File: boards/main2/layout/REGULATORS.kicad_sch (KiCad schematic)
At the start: 32 parts, among them IC7 L6981C33DR, J1 B02B-PASK(LF)(SN), Q6 HSBB3072, Q8 AO3401A, SW4 MK-12D18-G040, U8 ADP7142ACPZN3.3-R7, U9 INA228AIDGSR

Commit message: 🎨 Place main2's REGULATORS sheet
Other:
- note added: "3V3_A analog LDO: ADP7142, RC-filtered input"
- note added: "3V3_D buck: L6981C33, fixed 3.3 V"
- note added: "Battery current monitor: shunt R59, INA228 on the ESP32's I2C"
- note added: "Battery input and switch: SW4 drives the low-side MOSFET Q6"
- note added: "Battery voltage to the ADC"
- note added: "Power path: VSYS = VBAT or VBUS"
- note added: "Sheet ports"
- title: (none) -> Battery input, power path and regulators
- moved on the sheet: C52, C53, C54, C55, C56, C57, C58, C59, C63, C80, C81, C90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

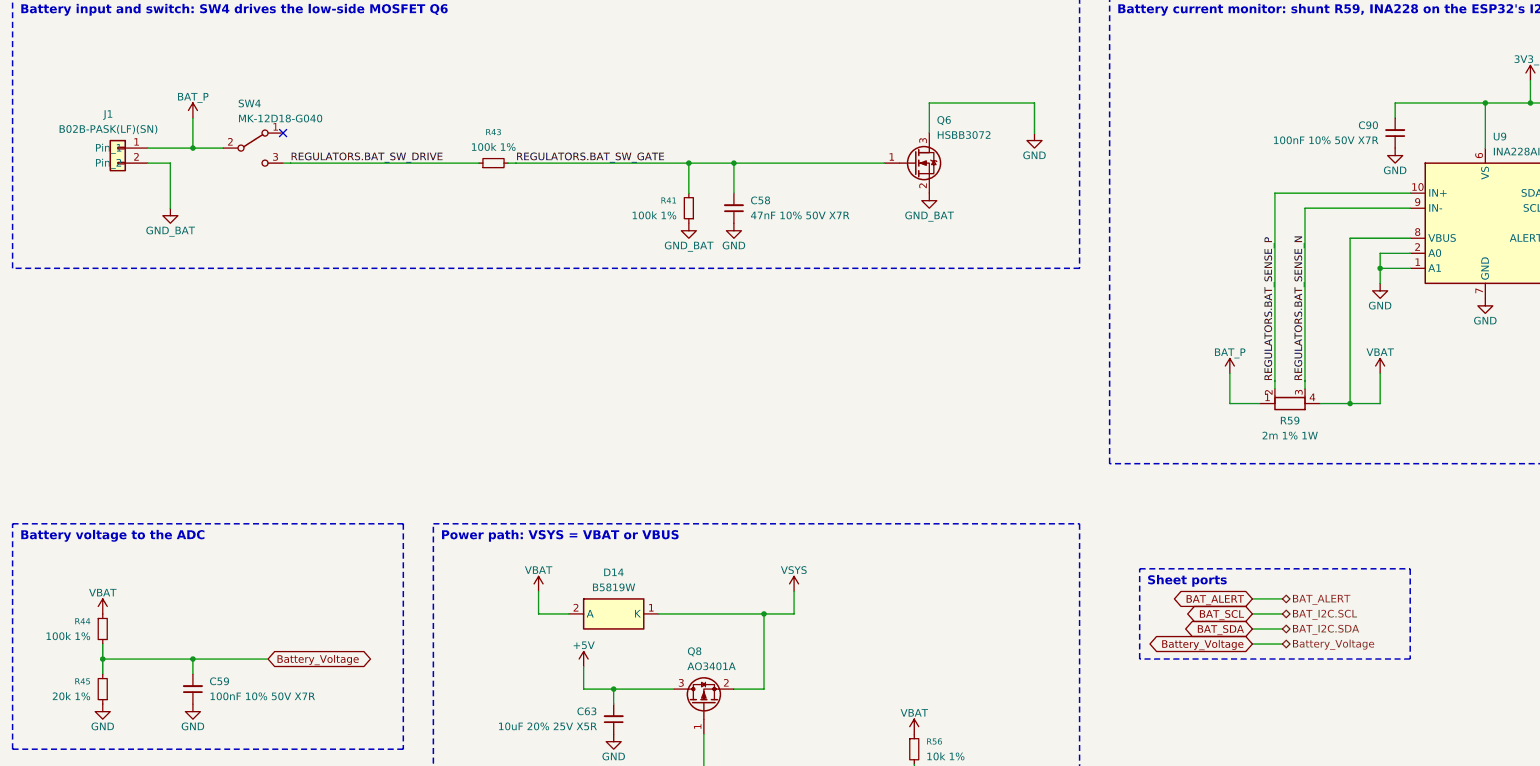
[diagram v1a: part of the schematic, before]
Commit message: 🎨 Place main2's SENSORS sheet, and draw the TLV9001's inputs as + and − in its triangle
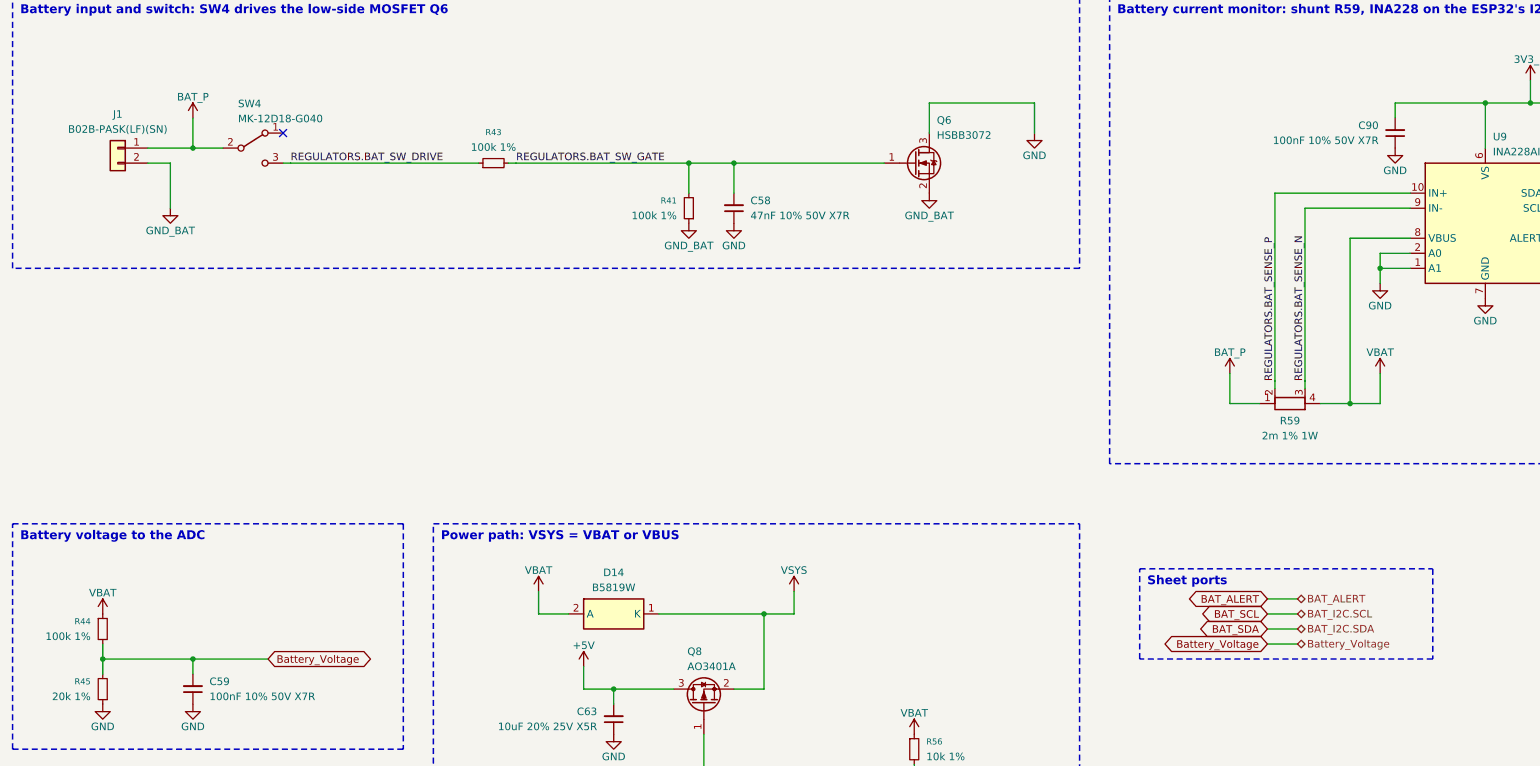
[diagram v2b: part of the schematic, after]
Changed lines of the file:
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@@
 		(dnp no)
 		(property "Reference" "J1"
-			(at 28.8955 34.925 0)
+			(at 30.48 34.925 0)
 			(show_name no)
 			(do_not_autoplace no)
@@
 		)
 		(property "Value" "B02B-PASK(LF)(SN)"
-			(at 28.8955 37.465 0)
+			(at 30.48 37.465 0)
 			(show_name no)
 			(do_not_autoplace no)
@@
 	(wire
 		(pts
-			(xy 222.25 116.84) (xy 227.33 116.84)
+			(xy 224.79 116.84) (xy 229.87 116.84)
 		)
 		(stroke
@@
 	(wire
 		(pts
-			(xy 222.25 119.38) (xy 227.33 119.38)
+			(xy 224.79 119.38) (xy 229.87 119.38)
 		)
 		(stroke
@@
 	(wire
 		(pts
-			(xy 222.25 121.92) (xy 227.33 121.92)
+			(xy 224.79 121.92) (xy 229.87 121.92)
 		)
 		(stroke
@@
 	(wire
 		(pts
-			(xy 222.25 124.46) (xy 227.33 124.46)
+			(xy 224.79 124.46) (xy 229.87 124.46)
 		)
 		(stroke
@@
 	(global_label "BAT_ALERT"
 		(shape bidirectional)
-		(at 222.25 116.84 180)
+		(at 224.79 116.84 180)
 		(effects
 			(font
@@
 		)
 		(property "Intersheetrefs" "${INTERSHEET_REFS}"
-			(at 222.25 116.84 0)
+			(at 224.79 116.84 0)
 			(hide yes)
 			(show_name no)
@@
 	(hierarchical_label "BAT_ALERT"
 		(shape bidirectional)
-		(at 227.33 116.84 0)
+		(at 229.87 116.84 0)
 		(effects
 			(font
@@
 	(global_label "BAT_SCL"
 		(shape bidirectional)
-		(at 222.25 119.38 180)
+		(at 224.79 119.38 180)
 		(effects
 			(font
@@
 		)
 		(property "Intersheetrefs" "${INTERSHEET_REFS}"
-			(at 222.25 119.38 0)
+			(at 224.79 119.38 0)
 			(hide yes)
 			(show_name no)
@@
 	(hierarchical_label "BAT_I2C.SCL"
 		(shape bidirectional)
-		(at 227.33 119.38 0)
+		(at 229.87 119.38 0)
 		(effects
 			(font
@@
 	(global_label "BAT_SDA"
 		(shape bidirectional)
-		(at 222.25 121.92 180)
+		(at 224.79 121.92 180)
 		(effects
 			(font
@@
 		)
 		(property "Intersheetrefs" "${INTERSHEET_REFS}"
-			(at 222.25 121.92 0)
+			(at 224.79 121.92 0)
 			(hide yes)
 			(show_name no)
@@
 	(hierarchical_label "BAT_I2C.SDA"
 		(shape bidirectional)
-		(at 227.33 121.92 0)
+		(at 229.87 121.92 0)
 		(effects
 			(font
@@
 	(global_label "Battery_Voltage"
 		(shape bidirectional)
-		(at 222.25 124.46 180)
+		(at 224.79 124.46 180)
 		(effects
 			(font
@@
 		)
 		(property "Intersheetrefs" "${INTERSHEET_REFS}"
-			(at 222.25 124.46 0)
+			(at 224.79 124.46 0)
 			(hide yes)
 			(show_name no)
@@
 	(hierarchical_label "Battery_Voltage"
 		(shape bidirectional)
-		(at 227.33 124.46 0)
+		(at 229.87 124.46 0)
 		(effects
 			(font
@@
 	(rectangle
 		(start 203.2 111.76)
-		(end 248.92 127)
+		(end 252.73 127)
 		(stroke
 			(width 0.254)

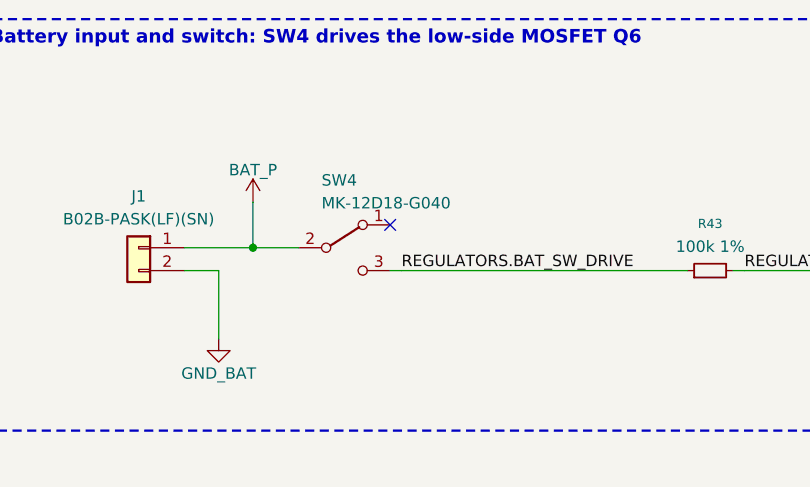
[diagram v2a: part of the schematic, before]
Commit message: 🔧 Switch main2's battery on the SK-12D29-G060, rated for the 4S pack
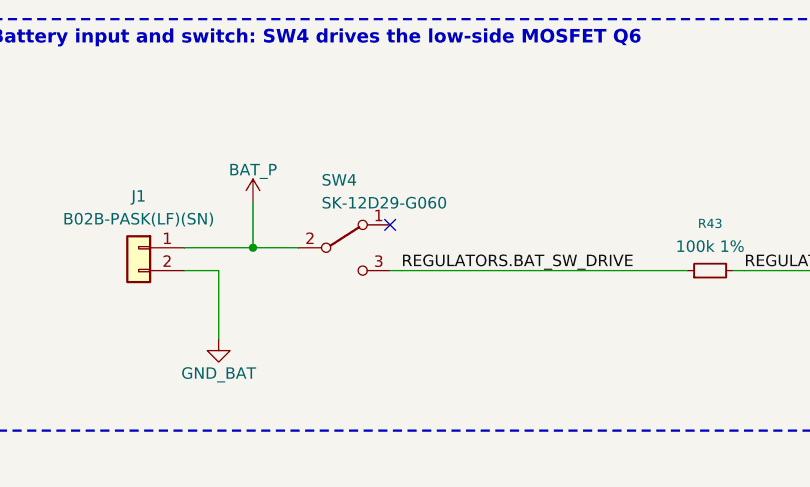
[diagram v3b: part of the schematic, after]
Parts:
- removed SW4: MK-12D18-G040, Team-Micras_MicrasPCB_components_g-switch_MK-12D18-G040:SW-TH_MK-12D18-G040, symbol MK-12D18-G040
- added SW4: SK-12D29-G060, Team-Micras_MicrasPCB_components_g-switch_SK-12D29-G060:SW-TH_SK-12D29-G060, symbol SK-12D29-G060
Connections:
- net BAT_P: now also SW4.2 (COM)
- net REGULATORS.BAT_SW_DRIVE: now also SW4.3 (B)
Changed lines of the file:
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@@
-	)
-	(symbol
-		(lib_id "MK-12D18-G040")
-		(at 53.34 40.64 0)
-		(unit 1)
-		(body_style 1)
-		(exclude_from_sim no)
-		(in_bom yes)
-		(on_board yes)
-		(in_pos_files yes)
-		(dnp no)
-		(property "Reference" "SW4"
-			(at 50.8 33.147 0)
-			(show_name no)
-			(do_not_autoplace no)
-			(effects
-				(font
-					(size 1.27 1.27)
-				)
-				(justify left)
-			)
-		)
-		(property "Value" "MK-12D18-G040"
-			(at 50.8 35.687 0)
-			(show_name no)
-			(do_not_autoplace no)
-			(effects
-				(font
-					(size 1.27 1.27)
-				)
-				(justify left)
-			)
-		)
-		(property "Footprint" "Team-Micras_MicrasPCB_components_g-switch_MK-12D18-G040:SW-TH_MK-12D18-G040"
-			(at 53.34 40.64 0)
-			(hide yes)
-			(show_name no)
-			(do_not_autoplace no)
-			(effects
-				(font
-					(size 1.27 1.27)
-				)
-			)
-		)
-		(property "Datasheet" "https://atta.szlcsc.com/upload/public/pdf/source/20201201/C963202_825FB742C5BA766BED52E1DDA96DE5A3.pdf"
-			(at 53.34 40.64 0)
-			(hide yes)
-			(show_name no)
-			(do_not_autoplace no)
-			(effects
-				(font
-					(size 1.27 1.27)
-				)
-			)
-		)
-		(property "Description" "SPDT right-angle slide switch, 4.0 mm actuator, DC 12 V 0.5 A / DC 6 V 1.0 A, through hole (G-Switch drawing MK-12D18-GXXX: position A joins pins 1-2, position B joins pins 2-3)"
-			(at 53.34 40.64 0)
-			(hide yes)
-			(show_name no)
-			(do_not_autoplace no)
-			(effects
-				(font
-					(size 1.27 1.27)
-				)
-			)
-		)
-		(property "Path" "REGULATORS.SW4.MK-12D18-G040"
-			(at 53.34 40.64 0)
-			(hide yes)
-			(show_name no)
-			(do_not_autoplace no)
-			(effects
-				(font
-					(size 1.27 1.27)
-				)
-			)
-		)
-		(pin "1"
-		)
-		(pin "2"
-		)
-		(pin "3"
-		)
-		(instances
-			(project "main2"
-				(path "/513d9cc1-d27a-514d-a37c-2f1ca04dddfa/f86c0649-bf57-58b2-a00a-5b8264913237"
-					(reference "SW4")
-					(unit 1)
-				)
-			)
-		)
 	)
 	(symbol
@@
 					(unit 1)
 				)
+			)
+		)
+	)
+	(symbol
+		(lib_id "SK-12D29-G060")
+		(at 53.34 40.64 0)
+		(unit 1)
+		(body_style 1)
+		(exclude_from_sim no)
+		(in_bom yes)
+		(on_board yes)
+		(in_pos_files yes)
+		(dnp no)
+		(property "Reference" "SW4"
+			(at 50.8 33.147 0)
+			(show_name no)
+			(do_not_autoplace no)
+			(effects
+				(font
+					(size 1.27 1.27)
+				)
+				(justify left)
+			)
+		)
+		(property "Value" "SK-12D29-G060"
+			(at 50.8 35.687 0)
+			(show_name no)
+			(do_not_autoplace no)
+			(effects
+				(font
+					(size 1.27 1.27)
+				)
+				(justify left)
+			)
+		)
+		(property "Footprint" "Team-Micras_MicrasPCB_components_g-switch_SK-12D29-G060:SW-TH_SK-12D29-G060"
+			(at 53.34 40.64 0)
+			(hide yes)
+			(show_name no)
+			(do_not_autoplace no)
+			(effects
+				(font
+					(size 1.27 1.27)
+				)
+			)
+		)
+		(property "Datasheet" "https://wmsc.lcsc.com/wmsc/upload/file/pdf/v2/lcsc/2108301530_G-Switch-SK-12D29-G060_C2848877.pdf"
+			(at 53.34 40.64 0)
+			(hide yes)
+			(show_name no)
+			(do_not_autoplace no)
+			(effects
+				(font
+					(size 1.27 1.27)
+				)
+			)
+		)
+		(property "Description" "SPDT right-angle slide switch, 6.0 mm lever, DC 24 V 1.0 A, through hole with two frame legs (G-Switch drawing SK-12D29-GXXX: the centre pin 2 is the common, the slider joins it to pin 1 or pin 3)"
+			(at 53.34 40.64 0)
+			(hide yes)
+			(show_name no)
+			(do_not_autoplace no)
+			(effects
+				(font
+					(size 1.27 1.27)
+				)
+			)
+		)
+		(property "Path" "REGULATORS.SW4.SK-12D29-G060"
+			(at 53.34 40.64 0)
+			(hide yes)
+			(show_name no)
+			(do_not_autoplace no)
+			(effects
+				(font
+					(size 1.27 1.27)
+				)
+			)
+		)
+		(pin "1"
+		)
+		(pin "2"
+		)
+		(pin "3"
+		)
+		(instances
+			(project "main2"
+				(path "/513d9cc1-d27a-514d-a37c-2f1ca04dddfa/f86c0649-bf57-58b2-a00a-5b8264913237"
+					(reference "SW4")
+					(unit 1)
+				)

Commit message: 🛡️ Clamp main2's battery input with an SMAJ18A across J1
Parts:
- added D15: 18V TVS 400W, Team-Micras_MicrasPCB_components_littelfuse_SMAJ18A:D_SMA, symbol SMAJ18A
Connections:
- net BAT_P: now also D15.1 (K)
- net GND_BAT: now also D15.2 (A)
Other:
- note added: "Battery input, TVS D15 and switch: SW4 drives the low-side MOSFET Q6"
- note removed: "Battery input and switch: SW4 drives the low-side MOSFET Q6"

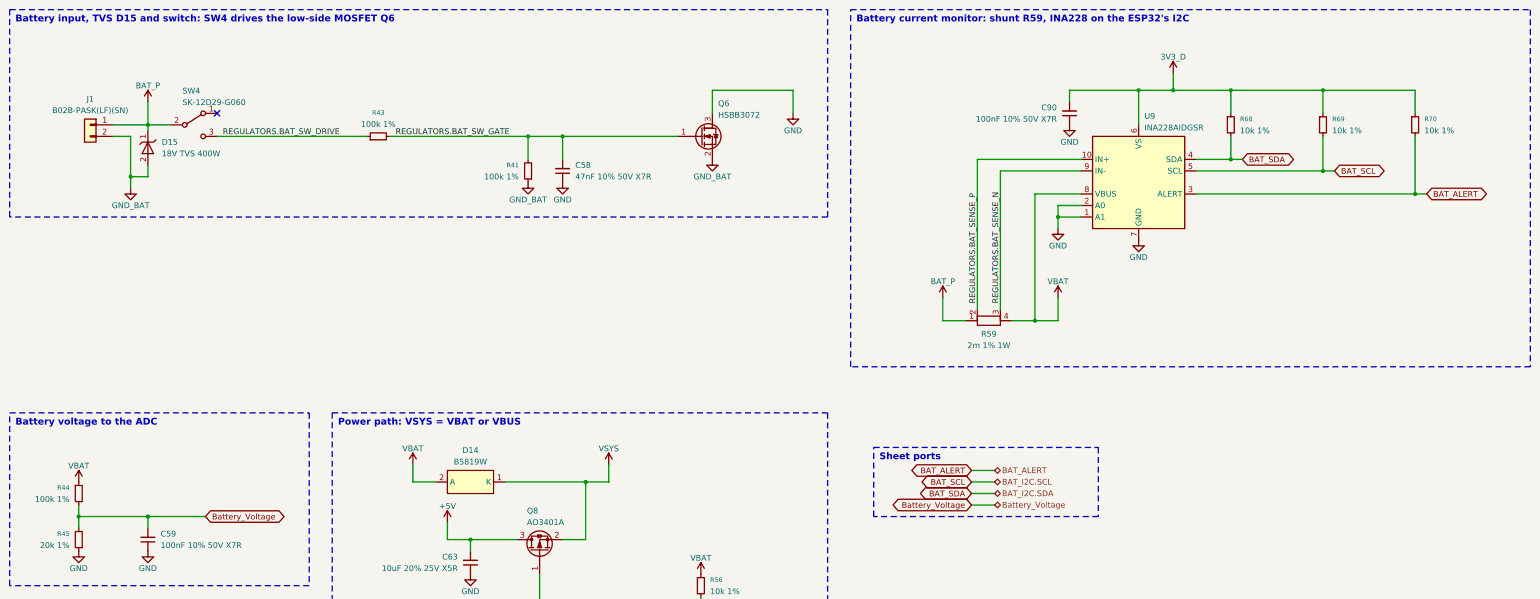
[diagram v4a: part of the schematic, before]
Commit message: ✨ Route main2 completely and fuse its battery input
- Every connection routed: short In2.Cu hops for digital STM32/ESP32 lines (never under
  switching or analog B.Cu copper, off the VBAT pour, out of the STM32 islands, In2 ground
  kept one plane), checked by a new layout test; F.Cu/B.Cu ground pours, ground stitching
  vias and teardrops.
- ADC pins swapped for the routing: Current_Sensor_Left on PB1 (fast channel), Wall_Sensor_0
  on PA4, Wall_Sensor_3 on PC0; firmware changes updated.
- Battery fuse F1 (Littelfuse 0501020.WR1, 20 A, 150 A at 32 VDC) from J1 to VBAT, the TVS and
  the switch drive behind it; the INA228 battery monitor and its shunt removed.
- route.py's DRC refills zones in KiCad, as the DRC gate does.
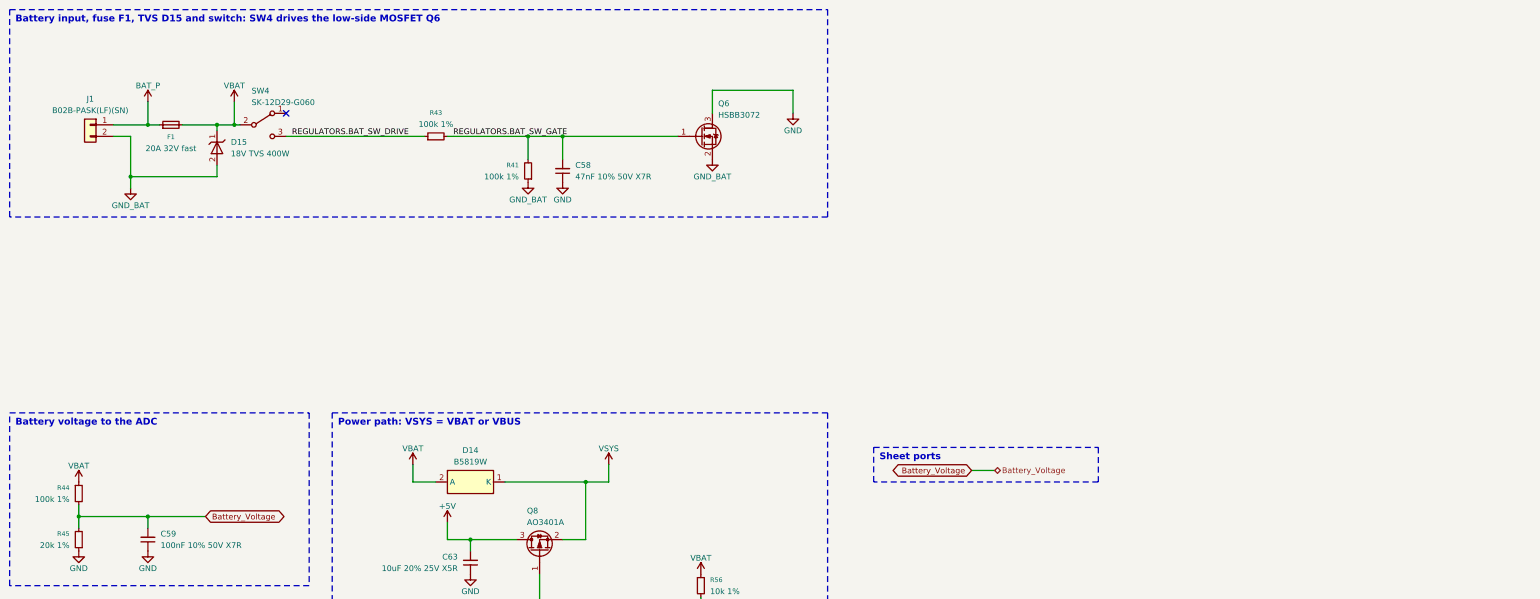
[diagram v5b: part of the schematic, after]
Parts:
- removed C90: 100nF 10% 50V X7R, stdlib_kicad-footprints_Capacitor_SMD:C_0402_1005Metric, symbol C_Small
- removed R59: 2m 1% 1W, Team-Micras_MicrasPCB_components_vishay_WSK2512-MID:Vishay_WSK2512_6332Metric_1mR-4m9R, symbol WSK2512-MID
- removed R68, R69, R70: 10k 1%, stdlib_kicad-footprints_Resistor_SMD:R_0402_1005Metric, symbol R_Small
- removed U9: INA228AIDGSR, Team-Micras_MicrasPCB_components_ti_INA228:Texas_DGS0010A_VSSOP-10_3x3mm_P0.5mm, symbol INA228
- added F1: 20A 32V fast, Team-Micras_MicrasPCB_components_littelfuse_0501020:Fuse_Littelfuse_501_1206, symbol 0501020
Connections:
- net BAT_P: now also F1.1; no longer D15.1 (K), SW4.2 (COM)
- net VBAT: now also D15.1 (K), SW4.2 (COM), F1.2
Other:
- note added: "Battery input, fuse F1, TVS D15 and switch: SW4 drives the low-side MOSFET Q6"
- note removed: "Battery current monitor: shunt R59, INA228 on the ESP32's I2C"
- note removed: "Battery input, TVS D15 and switch: SW4 drives the low-side MOSFET Q6"
- moved on the sheet: D15, R43, SW4
